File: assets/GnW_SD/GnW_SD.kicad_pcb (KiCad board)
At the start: 2 copper layers, 19.9 x 17.7 mm, 8 parts, among them U2 RT9193-28GB

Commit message: Board cleanup & finish
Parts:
- added Q**: Qwindelzorf, qwindelzorf:qwindelzorf_1520, B.Cu at (143.9, 83.7)
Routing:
- net Net-(Card1-CD/DAT3): track 16.9 -> 16.4 mm

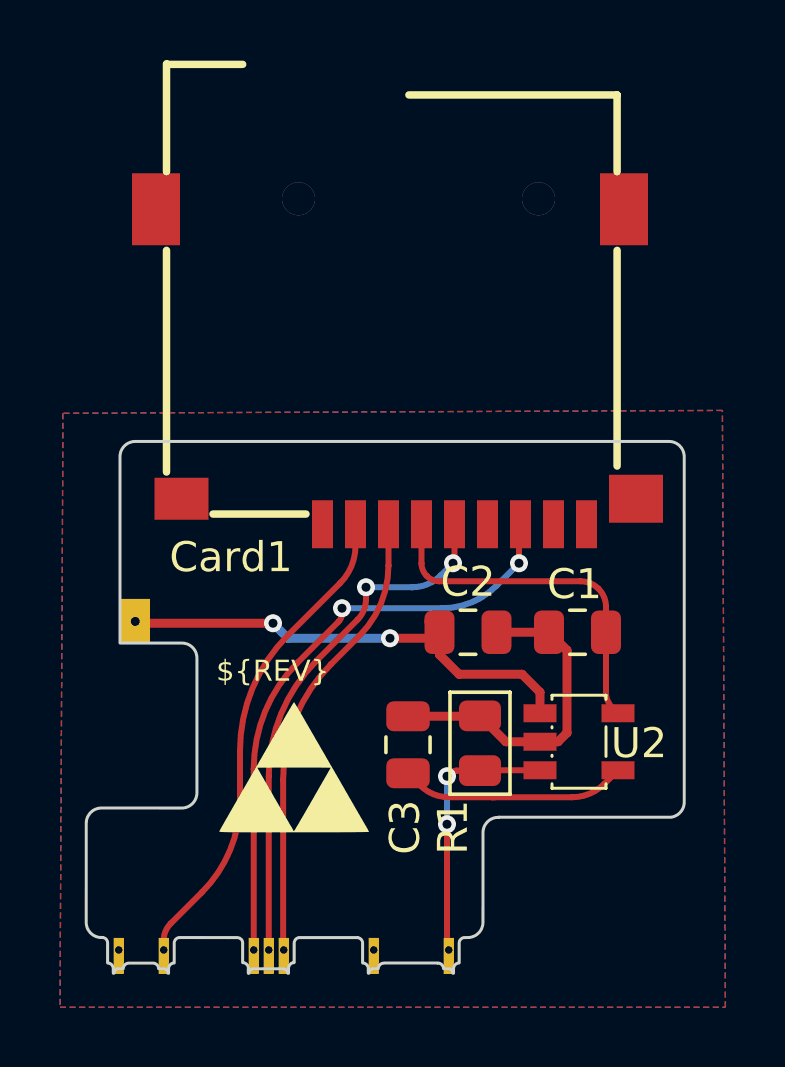
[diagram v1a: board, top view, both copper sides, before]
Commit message: Update LCSC part numbers
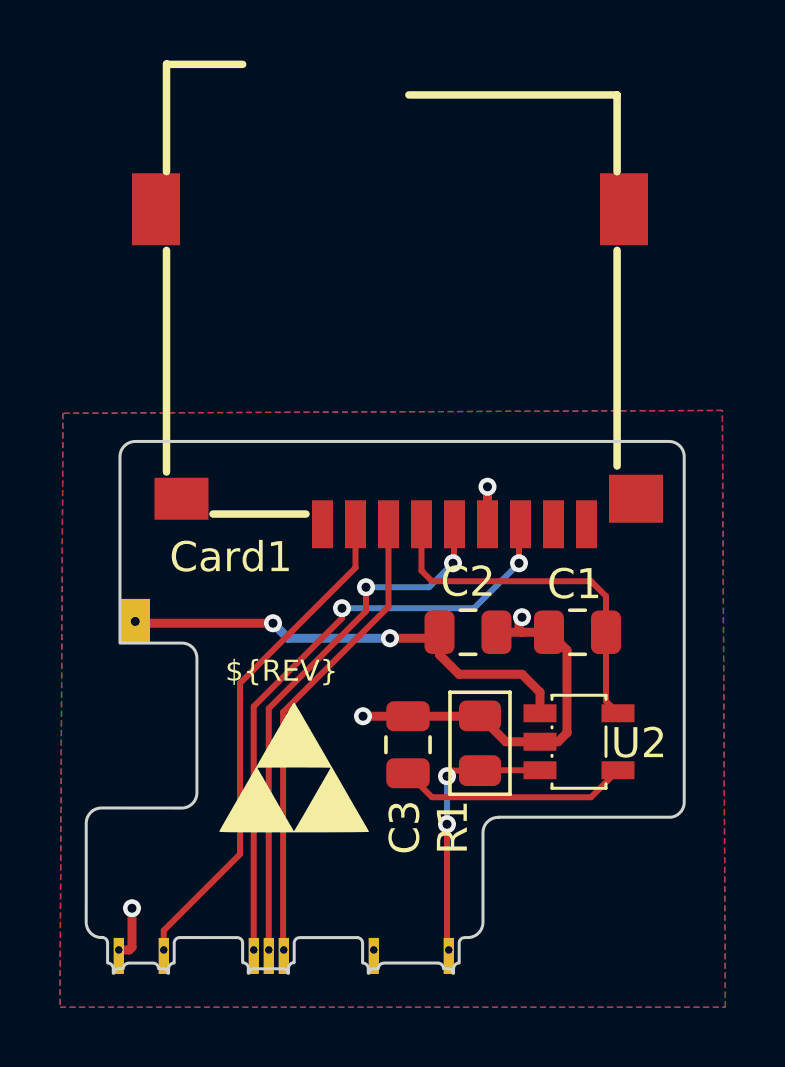
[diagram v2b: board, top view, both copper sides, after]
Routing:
- net GND: track 11.1 -> 16.3 mm, vias 0 -> 4
- net VDD: track 16.3 -> 15.8 mm
